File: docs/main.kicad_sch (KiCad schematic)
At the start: 8 parts, among them Q1 IRLB8743

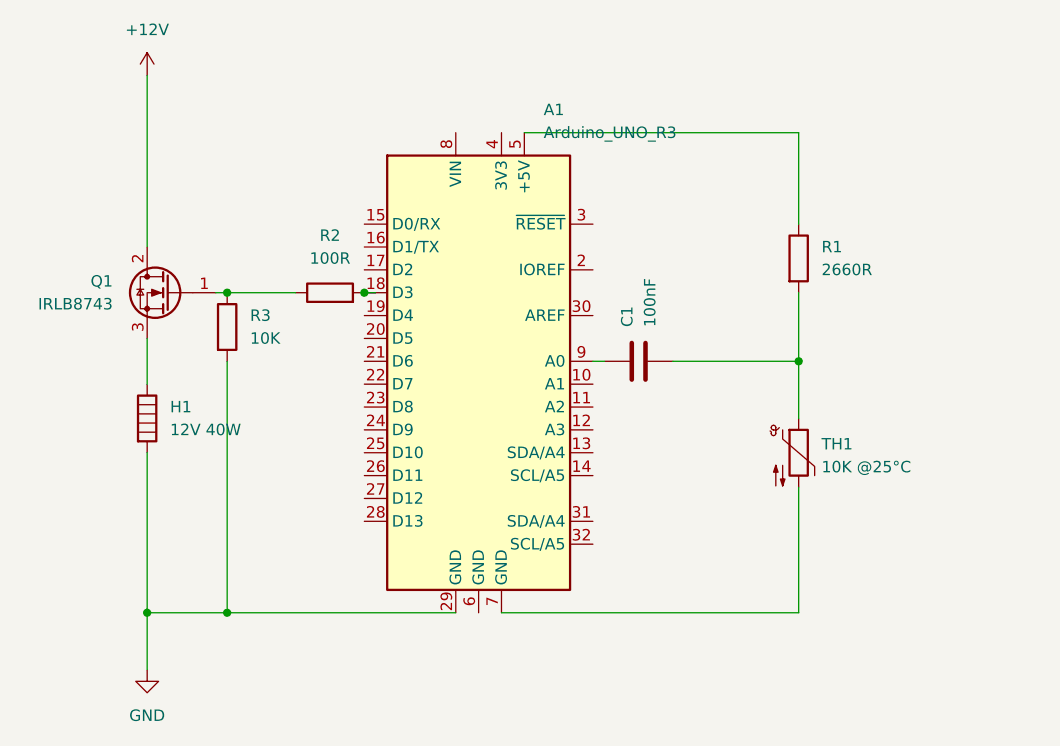
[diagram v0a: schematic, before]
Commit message: correcting main.kicad_sch
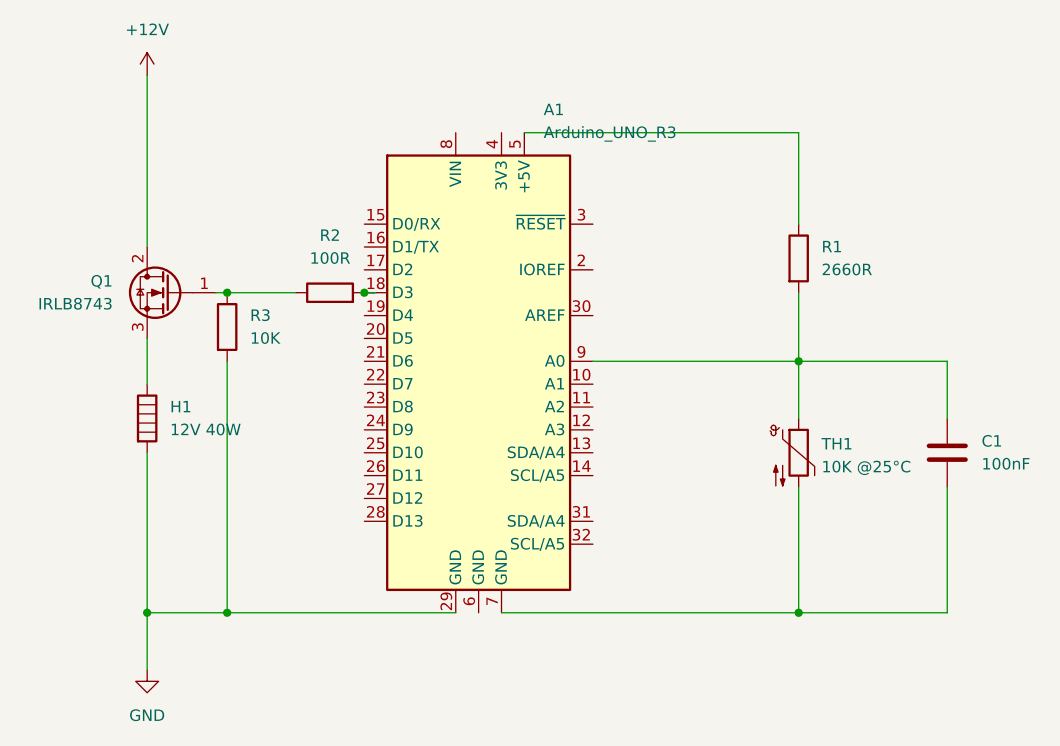
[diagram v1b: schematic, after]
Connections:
- net at A1.7 (GND), TH1.2: now also C1.2
- net at A1.9 (A0), C1.1: now also R1.2, TH1.1
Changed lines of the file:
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@@
 	(title_block
 		(title "pid-temperature-controller|main")
-		(date "2026-05-13")
-		(rev "v1.2")
+		(date "2026-09-22")
+		(rev "v1.3")
 	)
 	(junction
@@
 		(color 0 0 0 0)
 	)
+	(junction
+		(at 156.21 109.22)
+		(diameter 0)
+		(color 0 0 0 0)
+	)
 	(wire
 		(pts
@@
 	(wire
 		(pts
-			(xy 133.35 81.28) (xy 134.62 81.28)
+			(xy 133.35 81.28) (xy 156.21 81.28)
 		)
 		(stroke
@@
 	(wire
 		(pts
-			(xy 142.24 81.28) (xy 156.21 81.28)
+			(xy 172.72 81.28) (xy 172.72 87.63)
+		)
+		(stroke
+			(width 0)
+			(type default)
+		)
+	)
+	(wire
+		(pts
+			(xy 172.72 109.22) (xy 156.21 109.22)
 		)
 		(stroke
@@
 		(pts
 			(xy 83.82 109.22) (xy 83.82 115.57)
+		)
+		(stroke
+			(width 0)
+			(type default)
+		)
+	)
+	(wire
+		(pts
+			(xy 172.72 95.25) (xy 172.72 109.22)
+		)
+		(stroke
+			(width 0)
+			(type default)
+		)
+	)
+	(wire
+		(pts
+			(xy 156.21 81.28) (xy 172.72 81.28)
 		)
 		(stroke
@@
 	)
 	(symbol
-		(lib_id "Device:C")
-		(at 138.43 81.28 90)
-		(unit 1)
-		(body_style 1)
-		(exclude_from_sim no)
-		(in_bom yes)
-		(on_board yes)
-		(in_pos_files yes)
-		(dnp no)
-		(fields_autoplaced yes)
-		(property "Reference" "C1"
-			(at 137.1599 77.47 0)
-			(show_name no)
-			(do_not_autoplace no)
-			(effects
-				(font
-					(size 1.27 1.27)
-				)
-				(justify left)
-			)
-		)
-		(property "Value" "100nF"
-			(at 139.6999 77.47 0)
-			(show_name no)
-			(do_not_autoplace no)
-			(effects
-				(font
-					(size 1.27 1.27)
-				)
-				(justify left)
-			)
-		)
-		(property "Footprint" ""
-			(at 142.24 80.3148 0)
-			(hide yes)
-			(show_name no)
-			(do_not_autoplace no)
-			(effects
-				(font
-					(size 1.27 1.27)
-				)
-			)
-		)
-		(property "Datasheet" ""
-			(at 138.43 81.28 0)
-			(hide yes)
-			(show_name no)
-			(do_not_autoplace no)
-			(effects
-				(font
-					(size 1.27 1.27)
-				)
-			)
-		)
-		(property "Description" "Unpolarized capacitor"
-			(at 138.43 81.28 0)
-			(hide yes)
-			(show_name no)
-			(do_not_autoplace no)
-			(effects
-				(font
-					(size 1.27 1.27)
-				)
-			)
-		)
-		(pin "2"
-		)
-		(pin "1"
-		)
-		(instances
-			(project "main"
-				(path "/65a569c9-b81d-4fcf-906a-443098e8f4b2"
-					(reference "C1")
-					(unit 1)
-				)
-			)
-		)
-	)
-	(symbol
 		(lib_id "power:GND")
 		(at 83.82 115.57 0)
@@
 					(unit 1)
 				)
+			)
+		)
+	)
+	(symbol
+		(lib_id "Device:C")
+		(at 172.72 91.44 0)
+		(unit 1)
+		(body_style 1)
+		(exclude_from_sim no)
+		(in_bom yes)
+		(on_board yes)
+		(in_pos_files yes)
+		(dnp no)
+		(fields_autoplaced yes)
+		(property "Reference" "C1"
+			(at 176.53 90.1699 0)
+			(show_name no)
+			(do_not_autoplace no)
+			(effects
+				(font
+					(size 1.27 1.27)
+				)
+				(justify left)
+			)
+		)
+		(property "Value" "100nF"
+			(at 176.53 92.7099 0)
+			(show_name no)
+			(do_not_autoplace no)
+			(effects
+				(font
+					(size 1.27 1.27)
+				)
+				(justify left)
+			)
+		)
+		(property "Footprint" ""
+			(at 173.6852 95.25 0)
+			(hide yes)
+			(show_name no)
+			(do_not_autoplace no)
+			(effects
+				(font
+					(size 1.27 1.27)
+				)
+			)
+		)
+		(property "Datasheet" ""
+			(at 172.72 91.44 0)
+			(hide yes)
+			(show_name no)
+			(do_not_autoplace no)
+			(effects
+				(font
+					(size 1.27 1.27)
+				)
+			)
+		)
+		(property "Description" "Unpolarized capacitor"
+			(at 172.72 91.44 0)
+			(hide yes)
+			(show_name no)
+			(do_not_autoplace no)
+			(effects
+				(font
+					(size 1.27 1.27)
+				)
+			)
+		)
+		(pin "2"
+		)
+		(pin "1"
+		)
+		(instances
+			(project "main"
+				(path "/65a569c9-b81d-4fcf-906a-443098e8f4b2"
+					(reference "C1")
+					(unit 1)
+				)
